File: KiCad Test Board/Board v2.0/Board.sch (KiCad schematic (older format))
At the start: 28 parts, among them J1 Conn_01x11, J2 Screw_Terminal_01x04, U1 ADG732BSUZ

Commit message: Updated KiCad project files
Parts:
- C4: MPN 1206ZD104MAT2A -> QMK316BJ104KL-T
- C7: MPN 1206F104Z100CT -> C1206C104Z5VACTU
- R2: value 1M -> 1k; footprint Resistor_SMD:R_2512_6332Metric_Pad1.52x3.35mm_HandSolder -> Resistor_SMD:R_MiniMELF_MMA-0204; MPN SL1TTE1L00J -> MCF25SJR-1K; TC +180 PPM/C -> +200 PPM/C
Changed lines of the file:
@@
 P 3700 1300
 F 0 "R2" V 3500 1300 50  0000 C CNN
-F 1 "1M" V 3600 1300 50  0000 C CNN
-F 2 "Resistor_SMD:R_2512_6332Metric_Pad1.52x3.35mm_HandSolder" V 3630 1300 50  0001 C CNN
+F 1 "1k" V 3600 1300 50  0000 C CNN
+F 2 "Resistor_SMD:R_MiniMELF_MMA-0204" V 3630 1300 50  0001 C CNN
 F 3 "~" H 3700 1300 50  0001 C CNN
-F 4 "SL1TTE1L00J" V 3700 1300 50  0001 C CNN "MPN"
-F 5 "+180 PPM/C" V 3600 1650 50  0000 C CNN "TC"
+F 4 "MCF25SJR-1K" V 3700 1300 50  0001 C CNN "MPN"
+F 5 "+200 PPM/C" V 3600 1650 50  0000 C CNN "TC"
 	1    3700 1300
 	0    1    1    0
@@
 F 2 "Capacitor_SMD:C_1206_3216Metric_Pad1.42x1.75mm_HandSolder" H 8950 3800 50  0001 C CNN
 F 3 "~" H 8950 3800 50  0001 C CNN
-F 4 "1206F104Z100CT" V 8950 3800 50  0001 C CNN "MPN"
+F 4 "C1206C104Z5VACTU" V 8950 3800 50  0001 C CNN "MPN"
 F 5 "Y5V" V 8850 3600 50  0000 C CNN "TC"
 	1    8950 3800
@@
 F 2 "Capacitor_SMD:C_1206_3216Metric_Pad1.42x1.75mm_HandSolder" H 8950 2600 50  0001 C CNN
 F 3 "~" H 8950 2600 50  0001 C CNN
-F 4 "1206ZD104MAT2A" V 8950 2600 50  0001 C CNN "MPN"
+F 4 "QMK316BJ104KL-T" V 8950 2600 50  0001 C CNN "MPN"
 F 5 "X5R" V 8850 2400 50  0000 C CNN "TC"
 	1    8950 2600

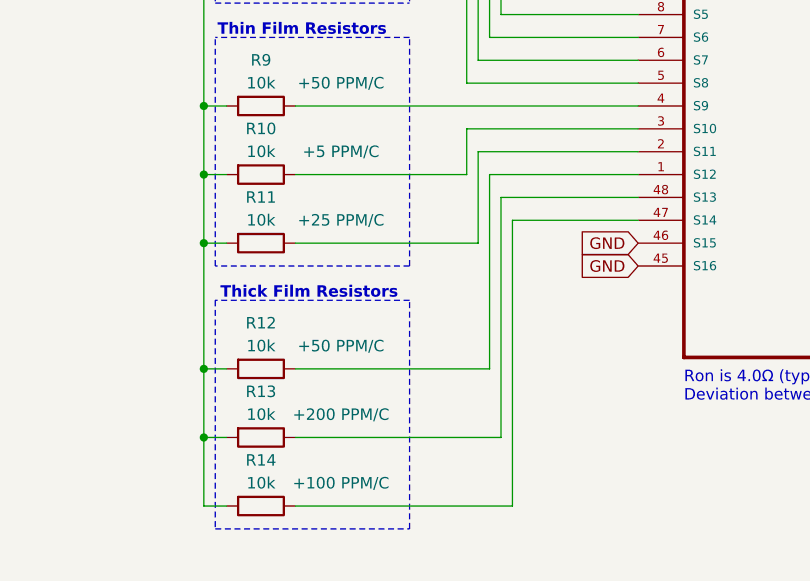
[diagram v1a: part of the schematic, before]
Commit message: Removed untested components
A bit late; removed unused components from schematic - not PCB
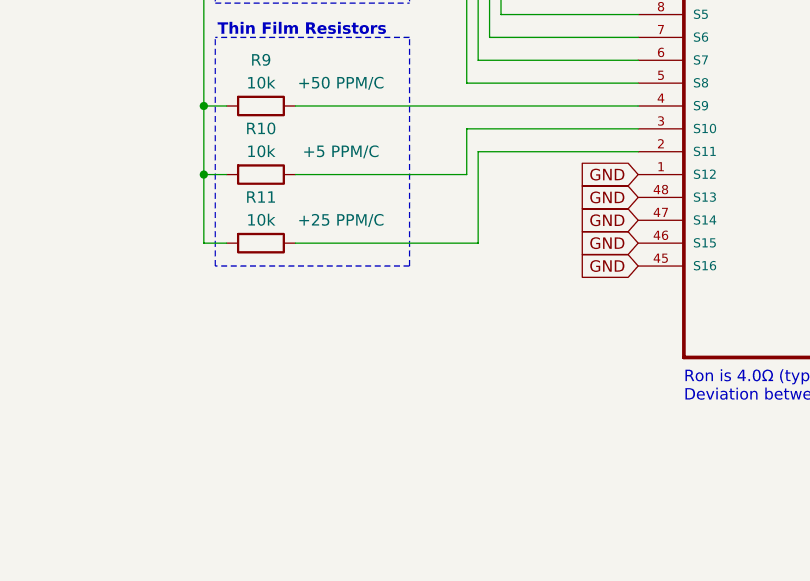
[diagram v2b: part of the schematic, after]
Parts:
- removed R12, R13, R14: 10k, Resistor_SMD:R_1206_3216Metric_Pad1.42x1.75mm_HandSolder, symbol Device:R
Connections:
- net GND: now also U1.1 (S12), U1.47 (S14), U1.48 (S13)
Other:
- note removed: "Thick Film Resistors\n"
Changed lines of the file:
@@
 Wire Notes Line
 	4350 2700 4350 3700
-Text Notes 4300 5000 2    50   ~ 10
-Thick Film Resistors\n
-$Comp
-L Device:R R14
-U 1 1 5DEE1E8B
-P 3700 5900
-F 0 "R14" V 3500 5900 50  0000 C CNN
-F 1 "10k" V 3600 5900 50  0000 C CNN
-F 2 "Resistor_SMD:R_1206_3216Metric_Pad1.42x1.75mm_HandSolder" V 3630 5900 50  0001 C CNN
-F 3 "~" H 3700 5900 50  0001 C CNN
-F 4 "RN73R2BTTD1001B05" V 3700 5900 50  0001 C CNN "MPN"
-F 5 "+100 PPM/C" V 3600 6250 50  0000 C CNN "TC"
-	1    3700 5900
-	0    1    1    0
-$EndComp
-$Comp
-L Device:R R13
-U 1 1 5DEE1E94
-P 3700 5600
-F 0 "R13" V 3500 5600 50  0000 C CNN
-F 1 "10k" V 3600 5600 50  0000 C CNN
-F 2 "Resistor_SMD:R_1206_3216Metric_Pad1.42x1.75mm_HandSolder" V 3630 5600 50  0001 C CNN
-F 3 "~" H 3700 5600 50  0001 C CNN
-F 4 "RN73H2BTTD1001B25" V 3700 5600 50  0001 C CNN "MPN"
-F 5 "+200 PPM/C" V 3600 5950 50  0000 C CNN "TC"
-	1    3700 5600
-	0    1    1    0
-$EndComp
-$Comp
-L Device:R R12
-U 1 1 5DEE1E9C
-P 3700 5300
-F 0 "R12" V 3500 5300 50  0000 C CNN
-F 1 "10k" V 3600 5300 50  0000 C CNN
-F 2 "Resistor_SMD:R_1206_3216Metric_Pad1.42x1.75mm_HandSolder" V 3630 5300 50  0001 C CNN
-F 3 "~" H 3700 5300 50  0001 C CNN
-F 4 "RN73H2BTTD1001B10" V 3700 5300 50  0001 C CNN "MPN"
-F 5 "+50 PPM/C" V 3600 5650 50  0000 C CNN "TC"
-	1    3700 5300
-	0    1    1    0
-$EndComp
-Wire Notes Line
-	3500 6000 4350 6000
-Wire Notes Line
-	4350 6000 4350 5000
 $Comp
 L Device:R R10
@@
 Wire Notes Line
 	4350 4850 3500 4850
-Wire Notes Line
-	3500 5000 3500 6000
-Wire Notes Line
-	4350 5000 3500 5000
 Wire Wire Line
 	3450 3600 3550 3600
 Connection ~ 3450 3600
 Wire Wire Line
-	3450 5900 3550 5900
-Wire Wire Line
 	3450 3600 3450 4150
 Wire Wire Line
-	3550 5600 3450 5600
-Connection ~ 3450 5600
-Wire Wire Line
-	3450 5600 3450 5900
-Wire Wire Line
-	3550 5300 3450 5300
-Connection ~ 3450 5300
-Wire Wire Line
-	3450 5300 3450 5600
-Wire Wire Line
 	3550 4750 3450 4750
-Connection ~ 3450 4750
-Wire Wire Line
-	3450 4750 3450 5300
 Wire Wire Line
 	3550 4450 3450 4450
@@
 	4650 4350 5350 4350
 Wire Wire Line
-	3850 5300 4700 5300
-Wire Wire Line
-	4700 5300 4700 4450
-Wire Wire Line
-	4700 4450 5350 4450
-Wire Wire Line
-	3850 5600 4750 5600
-Wire Wire Line
-	4750 5600 4750 4550
-Wire Wire Line
-	4750 4550 5350 4550
-Wire Wire Line
-	3850 5900 4800 5900
-Wire Wire Line
-	4800 5900 4800 4650
-Wire Wire Line
-	4800 4650 5350 4650
-Wire Wire Line
 	7150 3250 7400 3250
 Wire Wire Line
@@
 Wire Wire Line
 	9200 1150 9200 1600
+Text GLabel 5350 4650 0    50   Input ~ 0
+GND
+Text GLabel 5350 4550 0    50   Input ~ 0
+GND
+Text GLabel 5350 4450 0    50   Input ~ 0
+GND
 $EndSCHEMATC
